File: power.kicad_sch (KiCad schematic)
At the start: 3 parts, among them U5 AMS1117-3.3

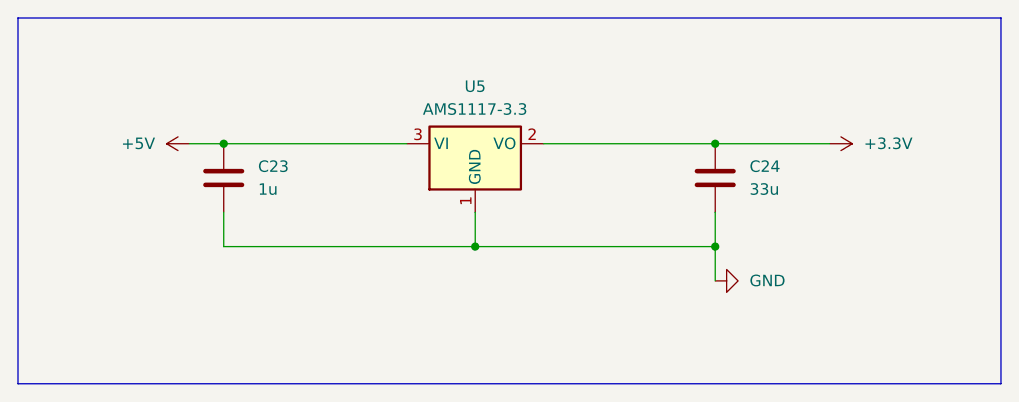
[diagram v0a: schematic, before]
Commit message: began fixing schematic added barometer
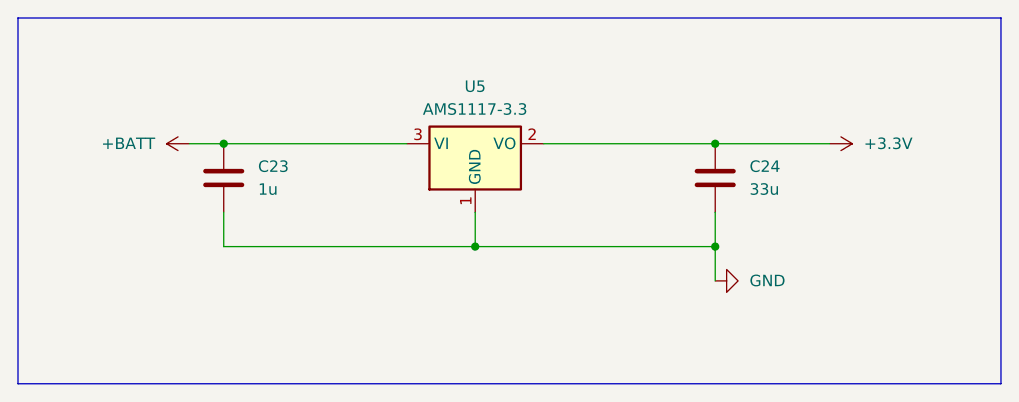
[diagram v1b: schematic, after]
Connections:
- net +5V renamed +BATT
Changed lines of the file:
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@@
-	)
-	(symbol
-		(lib_id "power:+5V")
-		(at 34.29 30.48 90)
-		(unit 1)
-		(exclude_from_sim no)
-		(in_bom yes)
-		(on_board yes)
-		(dnp no)
-		(fields_autoplaced yes)
-		(property "Reference" "#PWR043"
-			(at 38.1 30.48 0)
-			(effects
-				(font
-					(size 1.27 1.27)
-				)
-				(hide yes)
-			)
-		)
-		(property "Value" "+5V"
-			(at 30.48 30.4799 90)
-			(effects
-				(font
-					(size 1.27 1.27)
-				)
-				(justify left)
-			)
-		)
-		(property "Footprint" ""
-			(at 34.29 30.48 0)
-			(effects
-				(font
-					(size 1.27 1.27)
-				)
-				(hide yes)
-			)
-		)
-		(property "Datasheet" ""
-			(at 34.29 30.48 0)
-			(effects
-				(font
-					(size 1.27 1.27)
-				)
-				(hide yes)
-			)
-		)
-		(property "Description" "Power symbol creates a global label with name \"+5V\""
-			(at 34.29 30.48 0)
-			(effects
-				(font
-					(size 1.27 1.27)
-				)
-				(hide yes)
-			)
-		)
-		(pin "1"
-		)
-		(instances
-			(project "flightcomputer2"
-				(path "/6cb3dda3-5fe8-4715-b831-354360aa3199/ba4deb13-717a-43bb-a60d-abfd8de92de6"
-					(reference "#PWR043")
-					(unit 1)
-				)
-			)
-		)
 	)
 	(symbol
@@
 					(unit 1)
 				)
+			)
+		)
+	)
+	(symbol
+		(lib_id "power:+BATT")
+		(at 34.29 30.48 90)
+		(unit 1)
+		(exclude_from_sim no)
+		(in_bom yes)
+		(on_board yes)
+		(dnp no)
+		(fields_autoplaced yes)
+		(property "Reference" "#PWR05"
+			(at 38.1 30.48 0)
+			(effects
+				(font
+					(size 1.27 1.27)
+				)
+				(hide yes)
+			)
+		)
+		(property "Value" "+BATT"
+			(at 30.48 30.4799 90)
+			(effects
+				(font
+					(size 1.27 1.27)
+				)
+				(justify left)
+			)
+		)
+		(property "Footprint" ""
+			(at 34.29 30.48 0)
+			(effects
+				(font
+					(size 1.27 1.27)
+				)
+				(hide yes)
+			)
+		)
+		(property "Datasheet" ""
+			(at 34.29 30.48 0)
+			(effects
+				(font
+					(size 1.27 1.27)
+				)
+				(hide yes)
+			)
+		)
+		(property "Description" "Power symbol creates a global label with name \"+BATT\""
+			(at 34.29 30.48 0)
+			(effects
+				(font
+					(size 1.27 1.27)
+				)
+				(hide yes)
+			)
+		)
+		(pin "1"
+		)
+		(instances
+			(project ""
+				(path "/6cb3dda3-5fe8-4715-b831-354360aa3199/ba4deb13-717a-43bb-a60d-abfd8de92de6"
+					(reference "#PWR05")
+					(unit 1)
+				)
